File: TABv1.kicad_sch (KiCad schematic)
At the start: 39 parts, among them J10 Conn_02x03_Odd_Even, J11 Conn_UART_1, J5 Conn_02x06_Counter_Clockwise, J6 SWD, J9 Conn_02x03_Odd_Even, Q2 NMOS, SW2 RESET, U1 RP2350B-QFN80, Y1 12MHz

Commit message: perché non funziona
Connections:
- net PYRO_FIRE_4: no longer names the net of U1.48 (GPIO39)
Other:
- sheet Pyro ports: added none; removed PYRO_FIRE_4
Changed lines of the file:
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@@
 	(wire
 		(pts
-			(xy 148.59 162.56) (xy 129.54 162.56)
-		)
-		(stroke
-			(width 0)
-			(type default)
-		)
-	)
-	(wire
-		(pts
 			(xy 354.33 81.28) (xy 369.57 81.28)
 		)
@@
 		)
 	)
-	(wire
-		(pts
-			(xy 354.33 148.59) (xy 369.57 148.59)
-		)
-		(stroke
-			(width 0)
-			(type default)
-		)
-	)
 	(polyline
 		(pts
@@
 	(wire
 		(pts
+			(xy 354.33 146.05) (xy 369.57 146.05)
+		)
+		(stroke
+			(width 0)
+			(type default)
+		)
+	)
+	(wire
+		(pts
 			(xy 129.54 104.14) (xy 165.1 104.14)
 		)
@@
 		)
 	)
-	(wire
-		(pts
-			(xy 354.33 146.05) (xy 369.57 146.05)
-		)
-		(stroke
-			(width 0)
-			(type default)
-		)
-	)
 	(polyline
 		(pts
@@
 		)
 	)
-	(label "PYRO_FIRE_4"
-		(at 148.59 162.56 180)
-		(effects
-			(font
-				(size 1.27 1.27)
-			)
-			(justify right bottom)
-		)
-	)
 	(label "SD3"
 		(at 39.37 85.09 0)
@@
 	)
 	(label "PYRO_SENSE"
-		(at 354.33 148.59 0)
+		(at 354.33 146.05 0)
 		(effects
 			(font
@@
 		)
 	)
-	(label "PYRO_FIRE_4"
-		(at 354.33 146.05 0)
-		(effects
-			(font
-				(size 1.27 1.27)
-			)
-			(justify left bottom)
-		)
-	)
 	(label "L_GREEN"
 		(at 151.13 142.24 180)
@@
 	(sheet
 		(at 369.57 133.985)
-		(size 18.415 16.51)
+		(size 18.415 14.605)
 		(exclude_from_sim no)
 		(in_bom yes)
@@
 		)
 		(property "Sheetfile" "pyro.kicad_sch"
-			(at 369.57 151.0796 0)
+			(at 369.57 149.1746 0)
 			(effects
 				(font
@@
 			)
 		)
-		(pin "PYRO_FIRE_4" input
-			(at 369.57 146.05 180)
-			(effects
-				(font
-					(size 1.27 1.27)
-				)
-				(justify left)
-			)
-		)
 		(pin "PYRO_SENSE" input
-			(at 369.57 148.59 180)
+			(at 369.57 146.05 180)
 			(effects
 				(font

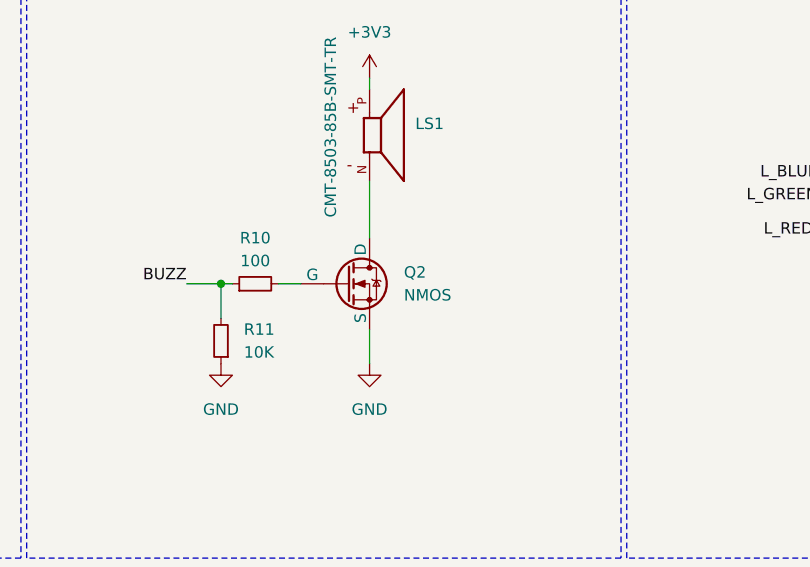
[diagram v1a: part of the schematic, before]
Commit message: connettori adattati
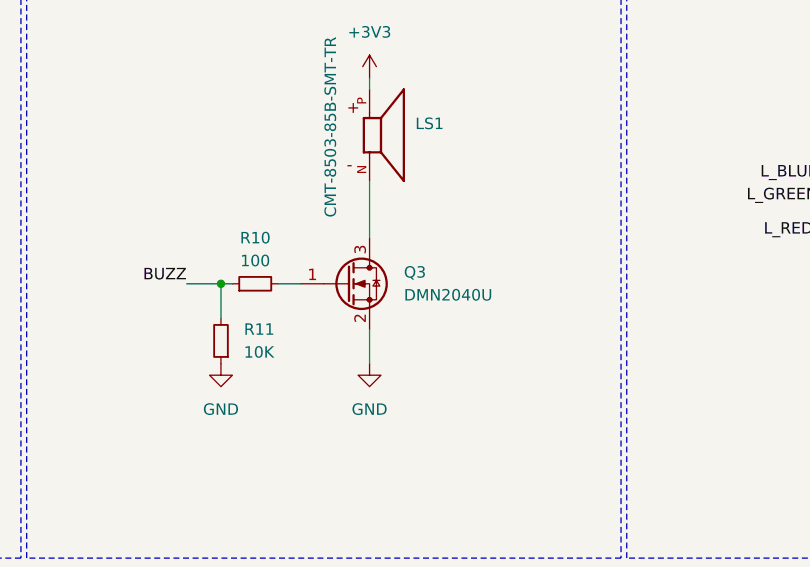
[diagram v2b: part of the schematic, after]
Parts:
- removed Q2: NMOS, Package_TO_SOT_SMD:SOT-23_Handsoldering, symbol Simulation_SPICE:NMOS
- added Q3: DMN2040U, Package_TO_SOT_SMD:SOT-23, symbol Transistor_FET:DMN2040U
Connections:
- net GND: now also Q3.2 (S)
- net at LS1.N: now also Q3.3 (D)
- net at R10.2: now also Q3.1 (G)
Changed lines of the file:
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@@
-	)
-	(symbol
-		(lib_id "Simulation_SPICE:NMOS")
-		(at 195.58 254 0)
-		(unit 1)
-		(exclude_from_sim no)
-		(in_bom yes)
-		(on_board yes)
-		(dnp no)
-		(fields_autoplaced yes)
-		(property "Reference" "Q2"
-			(at 201.93 252.7299 0)
-			(effects
-				(font
-					(size 1.27 1.27)
-				)
-				(justify left)
-			)
-		)
-		(property "Value" "NMOS"
-			(at 201.93 255.2699 0)
-			(effects
-				(font
-					(size 1.27 1.27)
-				)
-				(justify left)
-			)
-		)
-		(property "Footprint" "Package_TO_SOT_SMD:SOT-23_Handsoldering"
-			(at 200.66 251.46 0)
-			(effects
-				(font
-					(size 1.27 1.27)
-				)
-				(hide yes)
-			)
-		)
-		(property "Datasheet" "https://ngspice.sourceforge.io/docs/ngspice-html-manual/manual.xhtml#cha_MOSFETs"
-			(at 195.58 266.7 0)
-			(effects
-				(font
-					(size 1.27 1.27)
-				)
-				(hide yes)
-			)
-		)
-		(property "Description" "N-MOSFET transistor, drain/source/gate"
-			(at 195.58 254 0)
-			(effects
-				(font
-					(size 1.27 1.27)
-				)
-				(hide yes)
-			)
-		)
-		(property "Sim.Device" "NMOS"
-			(at 195.58 271.145 0)
-			(effects
-				(font
-					(size 1.27 1.27)
-				)
-				(hide yes)
-			)
-		)
-		(property "Sim.Type" "VDMOS"
-			(at 195.58 273.05 0)
-			(effects
-				(font
-					(size 1.27 1.27)
-				)
-				(hide yes)
-			)
-		)
-		(property "Sim.Pins" "1=D 2=G 3=S"
-			(at 195.58 269.24 0)
-			(effects
-				(font
-					(size 1.27 1.27)
-				)
-				(hide yes)
-			)
-		)
-		(pin "1"
-		)
-		(pin "2"
-		)
-		(pin "3"
-		)
-		(instances
-			(project ""
-				(path "/105f6e80-8e20-4d56-8eb3-6fa826818670"
-					(reference "Q2")
-					(unit 1)
-				)
-			)
-		)
 	)
 	(symbol
@@
 					(unit 1)
 				)
+			)
+		)
+	)
+	(symbol
+		(lib_id "Transistor_FET:DMN2040U")
+		(at 195.58 254 0)
+		(unit 1)
+		(exclude_from_sim no)
+		(in_bom yes)
+		(on_board yes)
+		(dnp no)
+		(fields_autoplaced yes)
+		(property "Reference" "Q3"
+			(at 201.93 252.7299 0)
+			(effects
+				(font
+					(size 1.27 1.27)
+				)
+				(justify left)
+			)
+		)
+		(property "Value" "DMN2040U"
+			(at 201.93 255.2699 0)
+			(effects
+				(font
+					(size 1.27 1.27)
+				)
+				(justify left)
+			)
+		)
+		(property "Footprint" "Package_TO_SOT_SMD:SOT-23"
+			(at 200.66 255.905 0)
+			(effects
+				(font
+					(size 1.27 1.27)
+					(italic yes)
+				)
+				(justify left)
+				(hide yes)
+			)
+		)
+		(property "Datasheet" "https://www.diodes.com/assets/Datasheets/DMN2040U.pdf"
+			(at 200.66 257.81 0)
+			(effects
+				(font
+					(size 1.27 1.27)
+				)
+				(justify left)
+				(hide yes)
+			)
+		)
+		(property "Description" "20V Vds, 6A Id, N-Channel MOSFET, SOT-23"
+			(at 195.58 254 0)
+			(effects
+				(font
+					(size 1.27 1.27)
+				)
+				(hide yes)
+			)
+		)
+		(pin "3"
+		)
+		(pin "2"
+		)
+		(pin "1"
+		)
+		(instances
+			(project ""
+				(path "/105f6e80-8e20-4d56-8eb3-6fa826818670"
+					(reference "Q3")
+					(unit 1)
+				)

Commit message: aggiornamenti rev 1.1
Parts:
- removed J6: SWD, Connector_PinHeader_2.54mm:PinHeader_1x03_P2.54mm_Vertical, symbol Connector:Conn_01x03_Pin
- added TP10, TP11, TP12, TP8, TP9: TestPoint_Flag, TestPoint:TestPoint_Pad_2.0x2.0mm, symbol Connector:TestPoint_Flag
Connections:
- net +3V3: now also TP9.1
- net GND: now also TP8.1
- net RESET: now also TP10.1
- net at U1.33 (SWCLK): now also TP11.1
- net at U1.34 (SWDIO): now also TP12.1

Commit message: fpc connector inizio
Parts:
- removed TP10, TP11, TP12, TP8, TP9: TestPoint_Flag, TestPoint:TestPoint_Pad_2.0x2.0mm, symbol Connector:TestPoint_Flag
- added J6: Conn_01x10_Socket, easyeda2kicad:FPC-SMD_XUNPU_FPC-0.5AD-10PB, symbol Connector:Conn_01x10_Socket
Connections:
- net +3V3: now also J6.9 (Pin_9)
- net GND: now also J6.10 (Pin_10)
- net RESET: now also J6.8 (Pin_8)
- net at U1.33 (SWCLK): now also J6.7 (Pin_7)
- net at U1.34 (SWDIO): now also J6.6 (Pin_6)
- new net SWDCLK_RADIO: J6.2 (Pin_2)
- new net SWDIO_RADIO: J6.3 (Pin_3)
- new net UART1_RX_RADIO: J6.5 (Pin_5)
- new net UART1_TX_RADIO: J6.4 (Pin_4)
- new net ~{USB_BOOT}: J6.1 (Pin_1)
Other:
- sheet LoRa & GPS ports: added SWCLK_RADIO, SWDIO_RADIO, UART1_RX_RADIO, UART1_TX_RADIO; removed none

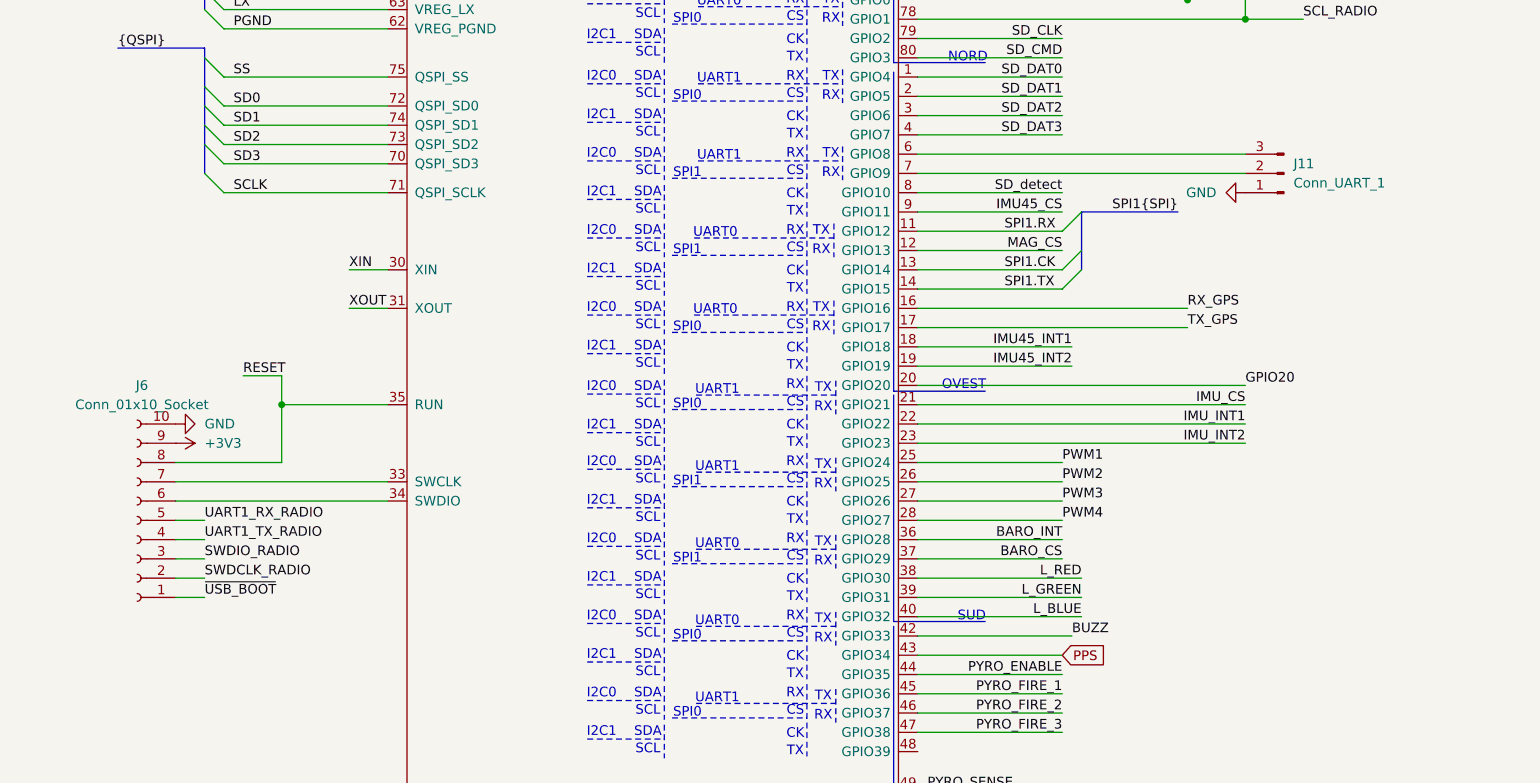
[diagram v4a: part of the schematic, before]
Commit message: spostato hardware in the loop  a connettore fpc e fixata etichetta bootsel
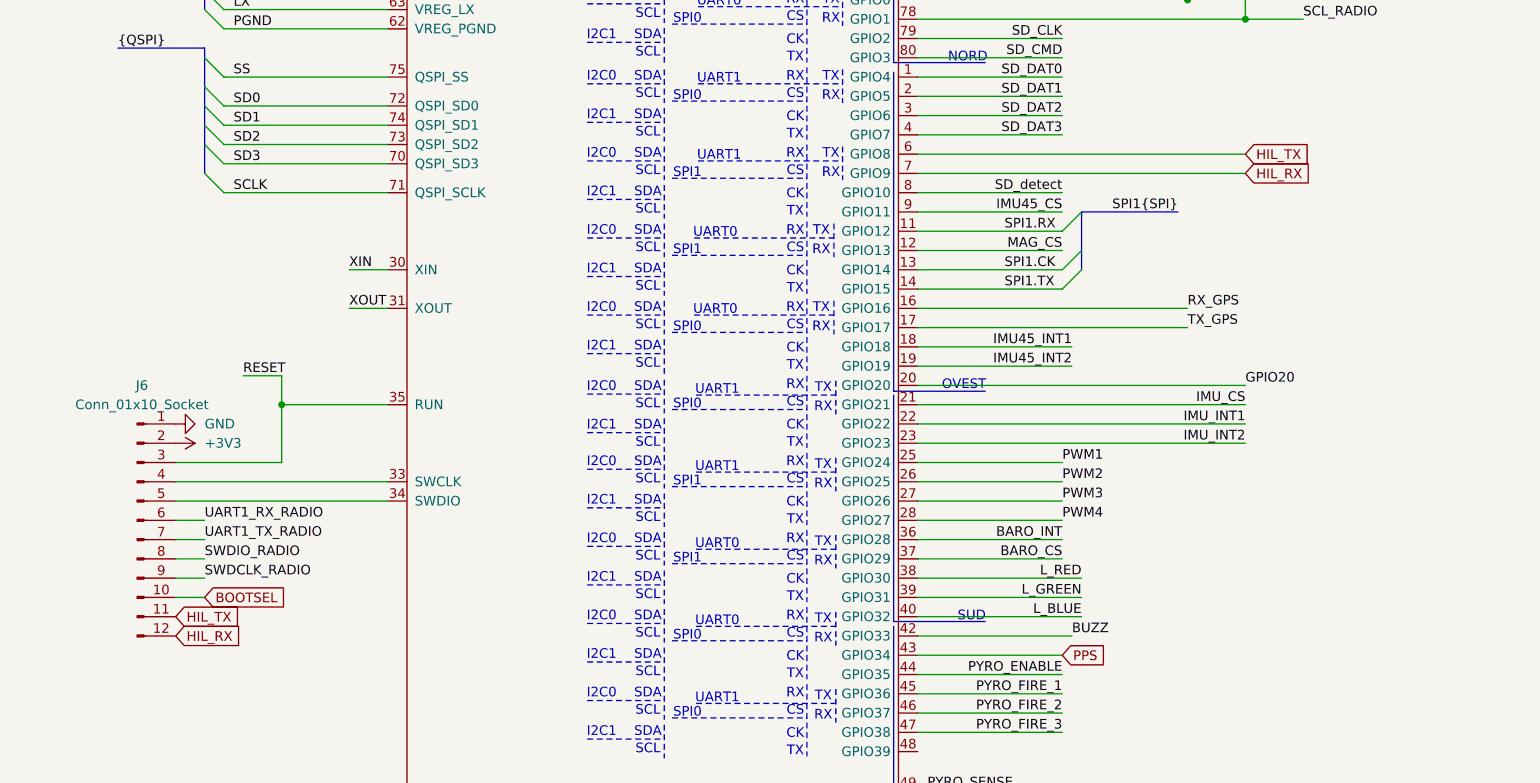
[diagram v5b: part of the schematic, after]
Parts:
- removed J11: Conn_UART_1, Connector_JST:JST_XH_B3B-XH-AM_1x03_P2.50mm_Vertical, symbol Connector:Conn_01x03_Pin
- J6: symbol Connector:Conn_01x10_Socket -> Connector:Conn_01x12_Pin
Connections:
- net ~{USB_BOOT} is gone; now on net GND: J6.1 (Pin_1)
- net +3V3: now also J6.2 (Pin_2); no longer J6.9 (Pin_9)
- net GND: no longer J6.10 (Pin_10)
- net RESET: now also J6.3 (Pin_3); no longer J6.8 (Pin_8)
- net SWDCLK_RADIO: now also J6.9 (Pin_9); no longer J6.2 (Pin_2)
- net SWDIO_RADIO: now also J6.8 (Pin_8); no longer J6.3 (Pin_3)
- net UART1_RX_RADIO: now also J6.6 (Pin_6); no longer J6.5 (Pin_5)
- net UART1_TX_RADIO: now also J6.7 (Pin_7); no longer J6.4 (Pin_4)
- net HIL_RX: now reaches U1.7 (GPIO9)
- net HIL_RX: now also J6.12 (Pin_12)
- net HIL_TX: now reaches U1.6 (GPIO8)
- net HIL_TX: now also J6.11 (Pin_11)
- net at U1.34 (SWDIO): now also J6.5 (Pin_5); no longer J6.6 (Pin_6)
- net at U1.33 (SWCLK): now also J6.4 (Pin_4); no longer J6.7 (Pin_7)
- new net BOOTSEL: J6.10 (Pin_10)
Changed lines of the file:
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@@
 		)
 	)
-	(label "~{USB_BOOT}"
-		(at 35.56 142.24 0)
-		(effects
-			(font
-				(size 1.27 1.27)
-			)
-			(justify left bottom)
-		)
-	)
 	(label "SD_DAT3"
 		(at 354.33 121.92 0)
@@
 		)
 	)
+	(global_label "HIL_TX"
+		(shape input)
+		(at 172.72 83.82 0)
+		(fields_autoplaced yes)
+		(effects
+			(font
+				(size 1.27 1.27)
+			)
+			(justify left)
+		)
+		(property "Intersheetrefs" "${INTERSHEET_REFS}"
+			(at 181.8133 83.82 0)
+			(effects
+				(font
+					(size 1.27 1.27)
+				)
+				(justify left)
+				(hide yes)
+			)
+		)
+	)
 	(global_label "D+"
 		(shape input)
@@
 		)
 	)
+	(global_label "HIL_RX"
+		(shape input)
+		(at 172.72 86.36 0)
+		(fields_autoplaced yes)
+		(effects
+			(font
+				(size 1.27 1.27)
+			)
+			(justify left)
+		)
+		(property "Intersheetrefs" "${INTERSHEET_REFS}"
+			(at 182.1157 86.36 0)
+			(effects
+				(font
+					(size 1.27 1.27)
+				)
+				(justify left)
+				(hide yes)
+			)
+		)
+	)
+	(global_label "HIL_RX"
+		(shape input)
+		(at 31.75 147.32 0)
+		(fields_autoplaced yes)
+		(effects
+			(font
+				(size 1.27 1.27)
+			)
+			(justify left)
+		)
+		(property "Intersheetrefs" "${INTERSHEET_REFS}"
+			(at 41.1457 147.32 0)
+			(effects
+				(font
+					(size 1.27 1.27)
+				)
+				(justify left)
+				(hide yes)
+			)
+		)
+	)
 	(global_label "D-"
 		(shape input)
@@
 		)
 	)
+	(global_label "BOOTSEL"
+		(shape input)
+		(at 35.56 142.24 0)
+		(fields_autoplaced yes)
+		(effects
+			(font
+				(size 1.27 1.27)
+			)
+			(justify left)
+		)
+		(property "Intersheetrefs" "${INTERSHEET_REFS}"
+			(at 46.8304 142.24 0)
+			(effects
+				(font
+					(size 1.27 1.27)
+				)
+				(justify left)
+				(hide yes)
+			)
+		)
+	)
+	(global_label "HIL_TX"
+		(shape input)
+		(at 31.75 144.78 0)
+		(fields_autoplaced yes)
+		(effects
+			(font
+				(size 1.27 1.27)
+			)
+			(justify left)
+		)
+		(property "Intersheetrefs" "${INTERSHEET_REFS}"
+			(at 40.8433 144.78 0)
+			(effects
+				(font
+					(size 1.27 1.27)
+				)
+				(justify left)
+				(hide yes)
+			)
+		)
+	)
 	(symbol
 		(lib_name "R_Small_1")
@@
 	)
 	(symbol
-		(lib_id "Connector:Conn_01x03_Pin")
-		(at 177.8 86.36 180)
-		(unit 1)
-		(exclude_from_sim no)
-		(in_bom yes)
-		(on_board yes)
-		(dnp no)
-		(fields_autoplaced yes)
-		(property "Reference" "J11"
-			(at 179.07 85.0899 0)
-			(effects
-				(font
-					(size 1.27 1.27)
-				)
-				(justify right)
-			)
-		)
-		(property "Value" "Conn_UART_1"
-			(at 179.07 87.6299 0)
-			(effects
-				(font
-					(size 1.27 1.27)
-				)
-				(justify right)
-			)
-		)
-		(property "Footprint" "Connector_JST:JST_XH_B3B-XH-AM_1x03_P2.50mm_Vertical"
-			(at 177.8 86.36 0)
-			(effects
-				(font
-					(size 1.27 1.27)
-				)
-				(hide yes)
-			)
-		)
-		(property "Datasheet" "~"
-			(at 177.8 86.36 0)
-			(effects
-				(font
-					(size 1.27 1.27)
-				)
-				(hide yes)
-			)
-		)
-		(property "Description" "Generic connector, single row, 01x03, script generated"
-			(at 177.8 86.36 0)
-			(effects
-				(font
-					(size 1.27 1.27)
-				)
-				(hide yes)
-			)
-		)
-		(pin "1"
-		)
-		(pin "2"
-		)
-		(pin "3"
-		)
-		(instances
-			(project "cockatiel"
-				(path "/105f6e80-8e20-4d56-8eb3-6fa826818670"
-					(reference "J11")
-					(unit 1)
-				)
-			)
-		)
-	)
-	(symbol
 		(lib_id "Device:C_Small")
 		(at 68.58 29.21 0)
@@
 	)
 	(symbol
-		(lib_id "Connector:Conn_01x10_Socket")
-		(at 26.67 132.08 180)
+		(lib_id "Connector:Conn_01x12_Pin")
+		(at 26.67 132.08 0)
 		(unit 1)
 		(exclude_from_sim no)
@@
 			)
 		)
-		(property "Description" "Generic connector, single row, 01x10, script generated"
+		(property "Description" "Generic connector, single row, 01x12, script generated"
 			(at 26.67 132.08 0)
 			(effects
@@
 		(pin "3"
 		)
+		(pin "12"
+		)
+		(pin "11"
+		)
 		(instances
 			(project ""
@@
 					(unit 1)
 				)
-			)
-		)
-	)
-	(symbol
-		(lib_id "power:GND")
-		(at 172.72 88.9 270)
-		(unit 1)
-		(exclude_from_sim no)
-		(in_bom yes)
-		(on_board yes)
-		(dnp no)
-		(fields_autoplaced yes)
-		(property "Reference" "#PWR028"
-			(at 166.37 88.9 0)
-			(effects
-				(font
-					(size 1.27 1.27)
-				)
-				(hide yes)
-			)
-		)
-		(property "Value" "GND"
-			(at 168.91 88.8999 90)
-			(effects
-				(font
-					(size 1.27 1.27)
-				)
-				(justify right)
-			)
-		)
-		(property "Footprint" ""
-			(at 172.72 88.9 0)
-			(effects
-				(font
-					(size 1.27 1.27)
-				)
-				(hide yes)
-			)
-		)
-		(property "Datasheet" ""
-			(at 172.72 88.9 0)
-			(effects
-				(font
-					(size 1.27 1.27)
-				)
-				(hide yes)
-			)
-		)
-		(property "Description" "Power symbol creates a global label with name \"GND\" , ground"
-			(at 172.72 88.9 0)
-			(effects
-				(font
-					(size 1.27 1.27)
-				)
-				(hide yes)
-			)
-		)
-		(pin "1"
-		)
-		(instances
-			(project "TABv1"
-				(path "/105f6e80-8e20-4d56-8eb3-6fa826818670"
-					(reference "#PWR028")
-					(unit 1)
-				)

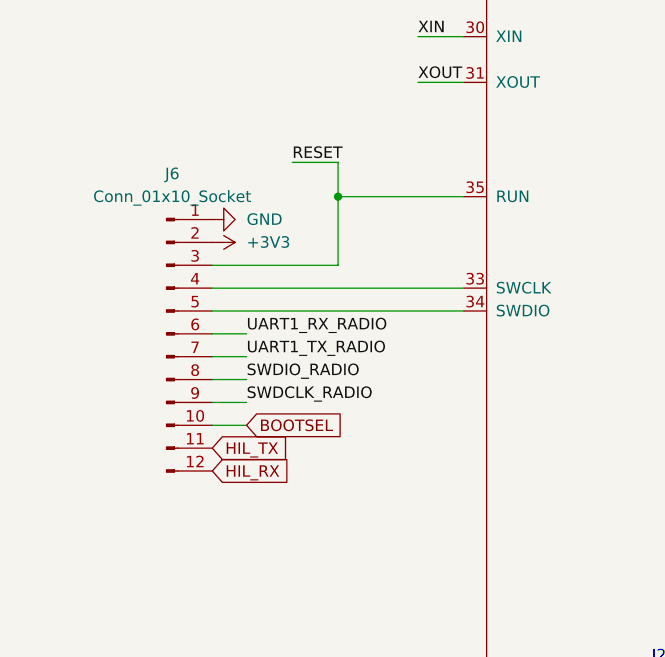
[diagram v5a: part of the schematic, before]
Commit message: fpc connector update
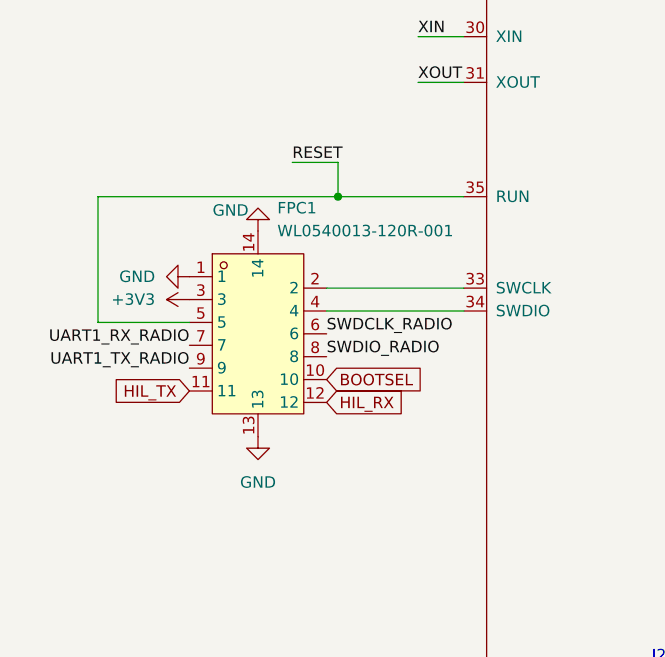
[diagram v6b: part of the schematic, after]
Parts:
- removed J6: Conn_01x10_Socket, easyeda2kicad:FPC-SMD_XUNPU_FPC-0.5AD-10PB, symbol Connector:Conn_01x12_Pin
- added FPC1: WL0540013-120R-001, easyeda2kicad:CONN-SMD_12P-WL0540013-120R-001, symbol easyeda2kicad_local:WL0540013-120R-001
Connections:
- net +3V3: now also FPC1.3
- net BOOTSEL: now also FPC1.10
- net GND: now also FPC1.1, FPC1.13, FPC1.14
- net HIL_RX: now also FPC1.12
- net HIL_TX: now also FPC1.11
- net RESET: now also FPC1.5
- net SWDCLK_RADIO: now also FPC1.6
- net SWDIO_RADIO: now also FPC1.8
- net UART1_RX_RADIO: now also FPC1.7
- net UART1_TX_RADIO: now also FPC1.9
- net at U1.33 (SWCLK): now also FPC1.2
- net at U1.34 (SWDIO): now also FPC1.4

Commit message: Tentativo di Sbroglio
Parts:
- removed FPC1: WL0540013-120R-001, easyeda2kicad:CONN-SMD_12P-WL0540013-120R-001, symbol easyeda2kicad_local:WL0540013-120R-001
- added H5, H6: MountingHole, MountingHole:MountingHole_3.2mm_M3, symbol Mechanical:MountingHole
- added J11, J6: Conn_02x06_Counter_Clockwise, Connector_PinHeader_2.54mm:PinHeader_2x06_P2.54mm_Vertical, symbol Connector_Generic:Conn_02x06_Odd_Even
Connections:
- net GPIO41: now also J11.7 (Pin_7)
- net GPIO42: now also J11.8 (Pin_8)
- net GPIO43: now also J11.9 (Pin_9)
- net GPIO44: now also J11.10 (Pin_10)
- net HIL_RX: now also J6.10 (Pin_10)
- net HIL_TX: now also J6.9 (Pin_9)
- net RX_GPS: now also J6.7 (Pin_7)
- net SCL_RADIO: now also J6.12 (Pin_12)
- net SDA_RADIO: now also J6.11 (Pin_11)
- net TX_GPS: now also J6.8 (Pin_8)
- net SWDCLK: now reaches U1.33 (SWCLK)
- net SWDCLK: now also J11.1 (Pin_1)
- net SWDIO: now reaches U1.34 (SWDIO)
- net SWDIO: now also J11.3 (Pin_3)
- net GPIO39: now reaches U1.48 (GPIO39)
- net GPIO39: now also J11.5 (Pin_5)
- net GPIO45: now reaches U1.56 (GPIO45_ADC5)
- net GPIO45: now also J11.12 (Pin_12)
- net GPIO46: now reaches U1.57 (GPIO46_ADC6)
- net GPIO46: now also J11.11 (Pin_11)
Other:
- note added: "Questi buchi servono in caso non volessimo fare delle viti passanti per i buchi principali"
